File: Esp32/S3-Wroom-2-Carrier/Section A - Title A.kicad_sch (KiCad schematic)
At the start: 1 part

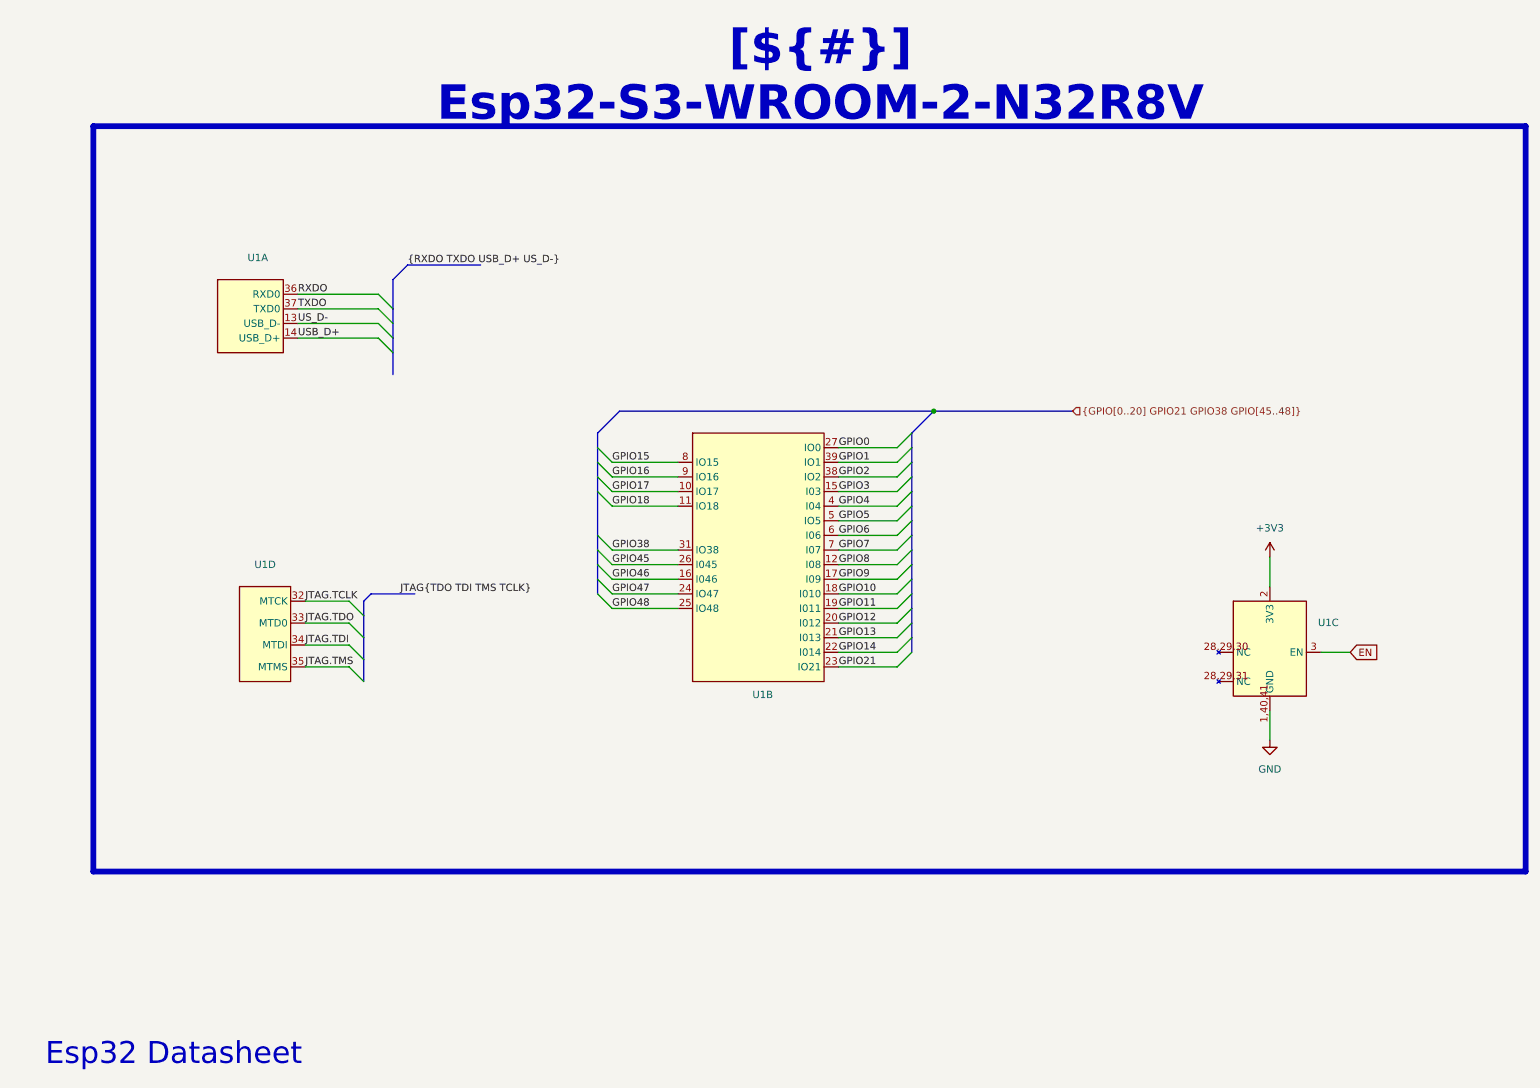
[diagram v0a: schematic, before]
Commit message: Power sheet
Added Esp32 power sheet and rename previous sheets
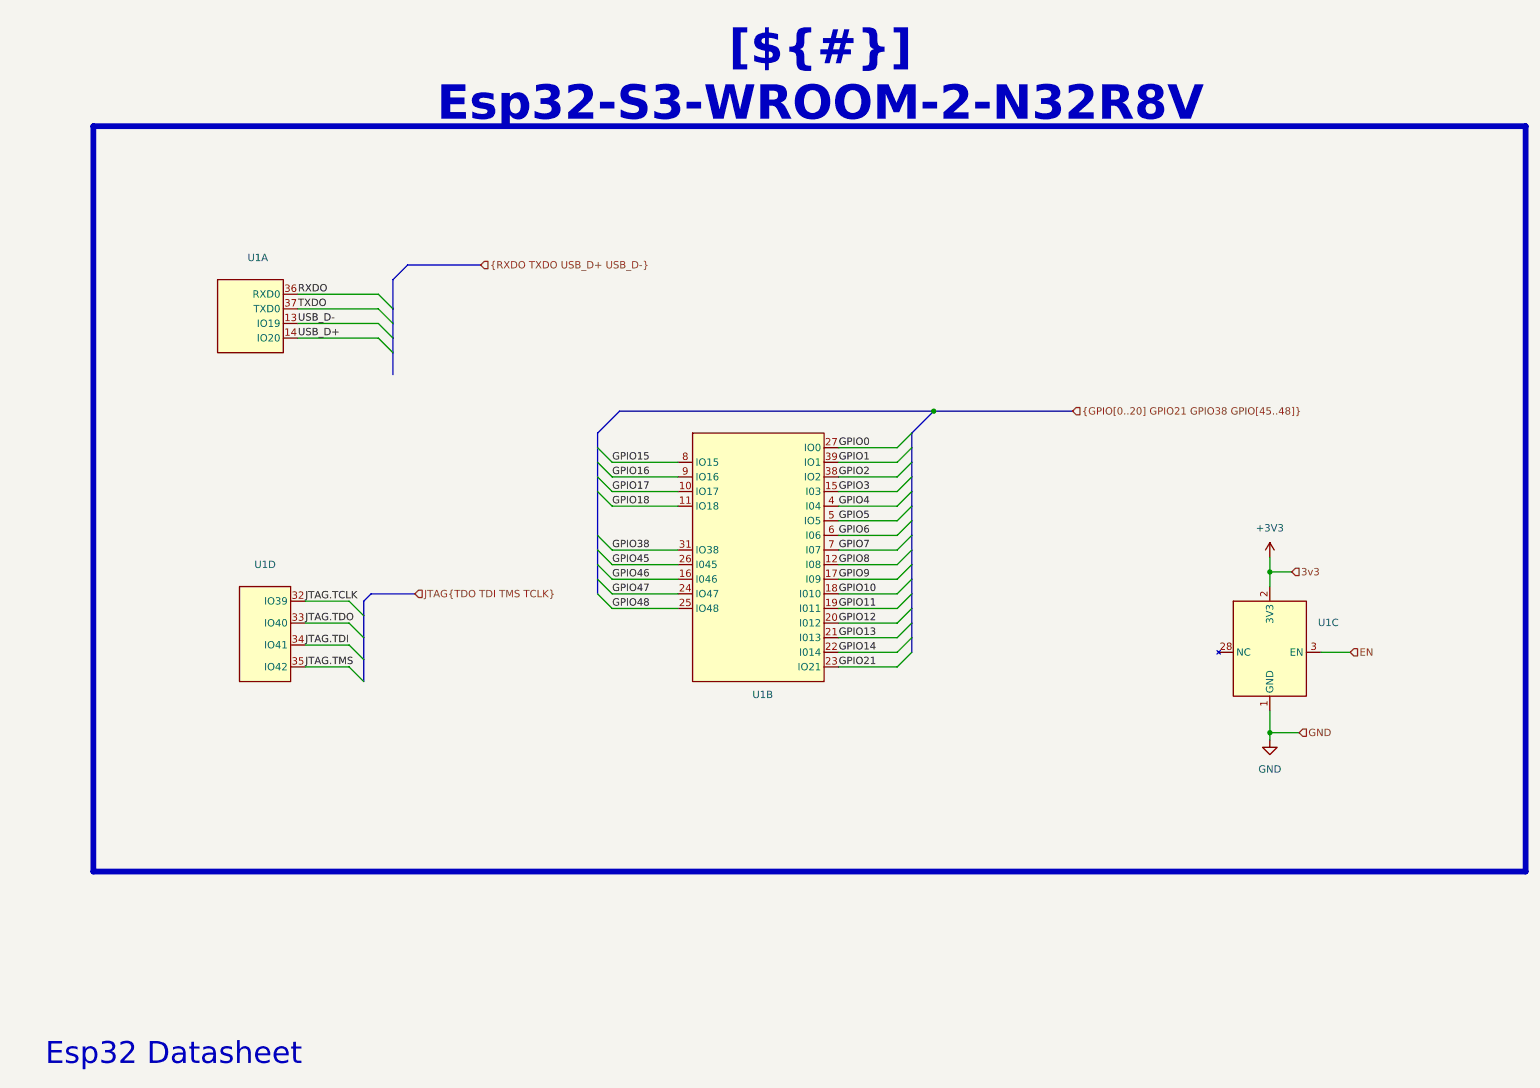
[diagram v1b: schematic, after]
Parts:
- U1: footprint (none) -> RF_Module:ESP32-S3-WROOM-2
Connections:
- net GND: now also U1.1 (GND), U1.40 (GND), U1.41 (GND); no longer U1.1,40,41 (GND)
- net US_D- renamed USB_D-
- new net: U1.28 (NC), U1.29 (NC), U1.30 (NC)

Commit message: Routing
Routing finished needs to be verify
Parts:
- added R5: 10K, Resistor_SMD:R_0805_2012Metric_Pad1.20x1.40mm_HandSolder, symbol Device:R_US
- U1: symbol Esp32-Carrier-Board:ESP32-S3-WROOM-2 -> _MCU_ESP32:ESP32-S3-WROOM-2
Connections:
- net +3V3: now also R5.1
- net EN: now also R5.2
- new net GPIO35: U1.28 (IO35)
- new net GPIO36: U1.29 (IO36)
- new net GPIO37: U1.30 (IO37)
